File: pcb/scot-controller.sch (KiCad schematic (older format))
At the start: 19 parts, among them IC1 MCP2562, J1 Conn_01x02_Female, J2 Conn_01x03_Female, J3 Conn_01x03_Female, U1 MCP1703A-5002_SOT223, U2 TSR_1-2465

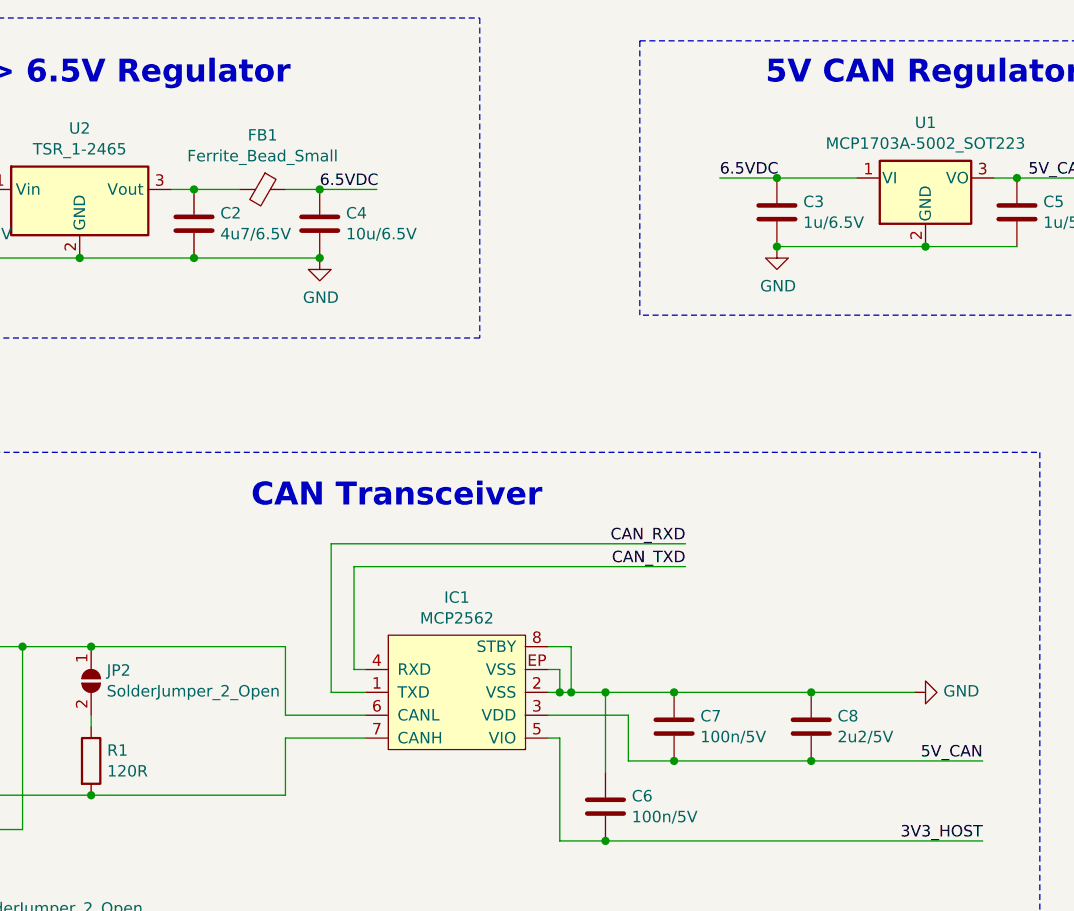
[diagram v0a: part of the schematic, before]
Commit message: pcb: Add BOM list. Adjust some values to reduce lines.
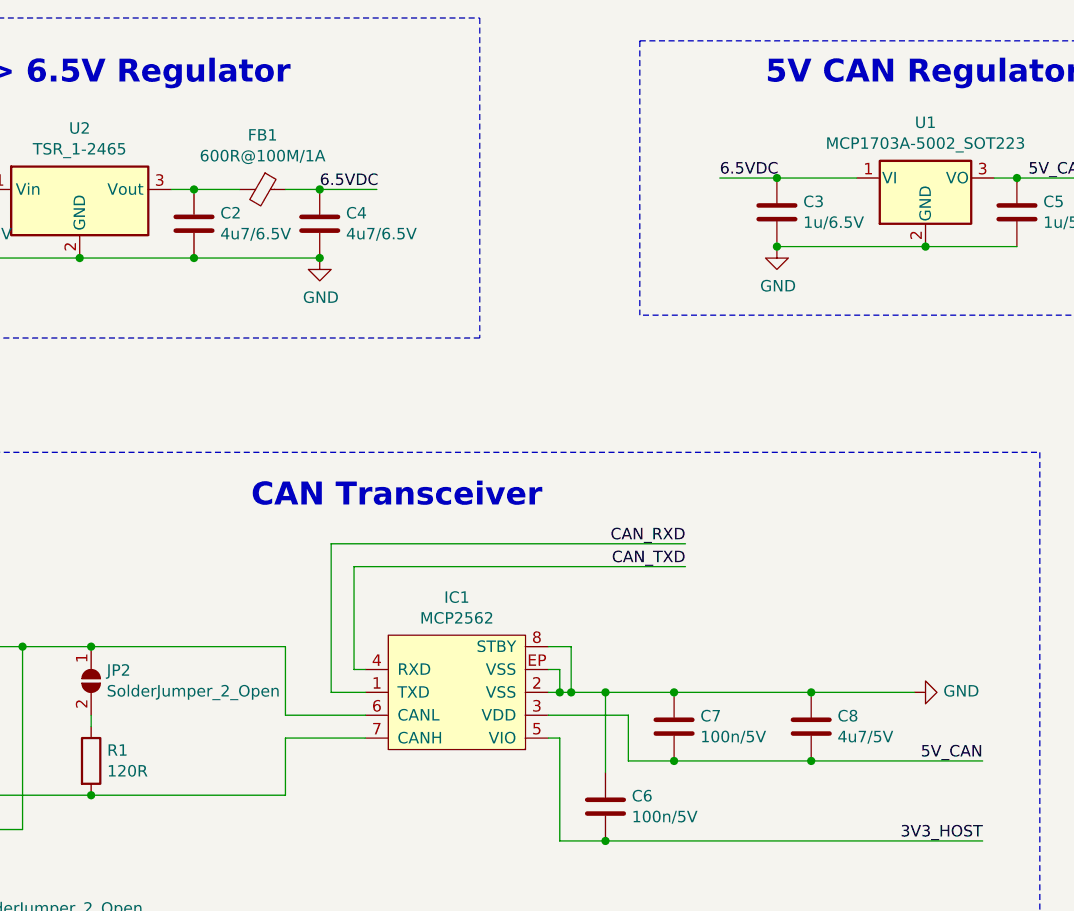
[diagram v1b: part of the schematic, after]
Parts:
- C4: value 10u/6.5V -> 4u7/6.5V
- C8: value 2u2/5V -> 4u7/5V
- FB1: value Ferrite_Bead_Small -> 600R@100M/1A
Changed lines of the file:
@@
 P 3450 2200
 F 0 "FB1" V 3213 2200 50  0000 C CNN
-F 1 "Ferrite_Bead_Small" V 3304 2200 50  0000 C CNN
+F 1 "600R@100M/1A" V 3304 2200 50  0000 C CNN
 F 2 "Inductor_SMD:L_0805_2012Metric_Pad1.15x1.40mm_HandSolder" V 3380 2200 50  0001 C CNN
 F 3 "~" H 3450 2200 50  0001 C CNN
@@
 P 3700 2350
 F 0 "C4" H 3815 2396 50  0000 L CNN
-F 1 "10u/6.5V" H 3815 2305 50  0000 L CNN
+F 1 "4u7/6.5V" H 3815 2305 50  0000 L CNN
 F 2 "Capacitor_SMD:C_0805_2012Metric_Pad1.15x1.40mm_HandSolder" H 3738 2200 50  0001 C CNN
 F 3 "~" H 3700 2350 50  0001 C CNN
@@
 P 5850 4550
 F 0 "C8" H 5965 4596 50  0000 L CNN
-F 1 "2u2/5V" H 5965 4505 50  0000 L CNN
+F 1 "4u7/5V" H 5965 4505 50  0000 L CNN
 F 2 "Capacitor_SMD:C_0805_2012Metric_Pad1.15x1.40mm_HandSolder" H 5888 4400 50  0001 C CNN
 F 3 "~" H 5850 4550 50  0001 C CNN

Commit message: pcb: Fix TXD/RXD mapping, move CAN regulator closer, add gitignore.
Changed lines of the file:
@@
 	9900 4350 10550 4350
 Text Label 10550 4350 2    50   ~ 0
-CAN_TXD
+CAN_RXD
 Wire Wire Line
 	9900 4450 10550 4450
 Text Label 10550 4450 2    50   ~ 0
-CAN_RXD
+CAN_TXD
 Wire Wire Line
 	2700 4850 2250 4850
